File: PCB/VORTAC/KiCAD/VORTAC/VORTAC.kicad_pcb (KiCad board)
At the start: 2 copper layers, 46 x 52.4 mm, 12 parts, among them J1 MillMax_004, J11 STEPPER, J12 IO, J13 918-418K2023S40001, J2 MillMax_004, J3 DOCK, J4 USB_HOST, J5 FAN_01, J6 FAN_02, J7 LED, J8 HOTEND, U1 STM32F103C8Tx

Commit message: footprints and libs
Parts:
- moved U1 9.61 mm to (76.7, 117.3)

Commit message: Schematic and Lib Updates
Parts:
- added C11: 0.1uF, Capacitor_SMD:C_0402_1005Metric_Pad0.74x0.62mm_HandSolder, F.Cu at (76.4, 135.0)
- added D1: D, Diode_SMD:D_SOD-123F, F.Cu at (47.1, 89.1)
- added D2: D, Diode_SMD:D_SOD-123F, F.Cu at (55.6, 82.7)
- added D3: D, Diode_SMD:D_SOD-123F, F.Cu at (52.6, 89.1)
- added D4: D, Diode_SMD:D_SOD-123F, F.Cu at (55.7, 78.5)
- added IC1: TMC2209-LA-T, ToolChanger:tmc_2209_package, F.Cu at (85.6, 112.6)
- added J10: FAN_01_V, Connector_PinHeader_1.27mm:PinHeader_2x03_P1.27mm_Vertical, F.Cu at (69.1, 132.6)
- added J14: FAN_02_V, Connector_PinHeader_1.27mm:PinHeader_2x03_P1.27mm_Vertical, F.Cu at (74.4, 129.5)
- added J15: LED_V, Connector_PinHeader_1.27mm:PinHeader_2x03_P1.27mm_Vertical, F.Cu at (94.1, 129.8)
- added J16: THERM_R, Connector_PinHeader_1.27mm:PinHeader_2x03_P1.27mm_Vertical, F.Cu at (82.6, 130.1)
- added J9: Conn_02x03_Odd_Even, ToolChanger:Molex_Micro-Fit_3.0_43045-0612_2x03_P3.00mm_Vertical, F.Cu at (102.0, 110.7)
- added Q1: WSD4066DN, ToolChanger:WSD4066DN, F.Cu at (68.5, 111.3)
- added Q2: WSD4066DN, ToolChanger:WSD4066DN, F.Cu at (116.7, 91.1)
- added Q3: WSD4066DN, ToolChanger:WSD4066DN, F.Cu at (68.5, 125.8)
- added Q4: Q_NMOS_GSD, ToolChanger:IRF9310PbF-1_SO-8, F.Cu at (93.7, 122.5)
- added Q5: Q_NPN_BEC, Package_TO_SOT_SMD:SOT-23, F.Cu at (91.9, 104.6)
- added Q6: Q_PNP_BEC, Package_TO_SOT_SMD:SOT-23, F.Cu at (95.8, 104.5)
- added Q7: Q_NMOS_GSD, ToolChanger:IRF9310PbF-1_SO-8, F.Cu at (93.8, 109.3)
- added Q8: Q_PMOS_GSD, ToolChanger:IRF9310PbF-1_SO-8, F.Cu at (94.0, 115.1)
- added R1: 5.12K, Resistor_SMD:R_0402_1005Metric, F.Cu at (59.1, 108.7)
- added R10: 10K, Resistor_SMD:R_0402_1005Metric, F.Cu at (49.0, 126.3)
- added R11: 10K, Resistor_SMD:R_0402_1005Metric, F.Cu at (51.8, 110.7)
- added R12: 10K, Resistor_SMD:R_0402_1005Metric, F.Cu at (51.8, 112.7)
- added R13: 10K, Resistor_SMD:R_0402_1005Metric, F.Cu at (46.0, 122.9)
- added R14: 100R, Resistor_SMD:R_0402_1005Metric, F.Cu at (51.8, 114.6)
- added R15: 10K, Resistor_SMD:R_0402_1005Metric, F.Cu at (50.5, 118.4)
- added R2: 5.12K, Resistor_SMD:R_0402_1005Metric, F.Cu at (62.1, 108.7)
- added R22: 220K, Resistor_SMD:R_0402_1005Metric, F.Cu at (54.2, 85.4)
- added R23: 220K, Resistor_SMD:R_0402_1005Metric, F.Cu at (57.2, 85.4)
- added R24: 220K, Resistor_SMD:R_0402_1005Metric, F.Cu at (56.8, 87.4)
- added R25: 220K, Resistor_SMD:R_0402_1005Metric, F.Cu at (59.7, 87.4)
- added R26: 220K, Resistor_SMD:R_0402_1005Metric, F.Cu at (56.8, 89.3)
- added R27: 220K, Resistor_SMD:R_0402_1005Metric, F.Cu at (60.1, 85.4)
- added R28: 10K, Resistor_SMD:R_0402_1005Metric, F.Cu at (79.5, 135.0)
- added R3: 100R, Resistor_SMD:R_0402_1005Metric, F.Cu at (51.7, 126.5)
- added R4: 100R, Resistor_SMD:R_0402_1005Metric, F.Cu at (48.9, 122.9)
- added R5: 100R, Resistor_SMD:R_0402_1005Metric, F.Cu at (46.5, 108.9)
- added R6: 100R, Resistor_SMD:R_0402_1005Metric, F.Cu at (46.1, 126.3)
- added R7: 100R, Resistor_SMD:R_0402_1005Metric, F.Cu at (43.2, 126.3)
- added R8: 100R, Resistor_SMD:R_0402_1005Metric, F.Cu at (40.3, 127.5)
- added R9: 10K, Resistor_SMD:R_0402_1005Metric, F.Cu at (40.3, 125.5)
- added U2: ADXL343, Package_LGA:LGA-14_3x5mm_P0.8mm_LayoutBorder1x6y, F.Cu at (66.7, 142.6)
- moved J3 23.9 mm to (123.7, 89.6)
- moved J13 22.3 mm to (72.8, 103.7)
- moved U1 0.82 mm to (76.2, 117.9)
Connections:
- net MCU_D+ renamed USBMCU_D+
- net MCU_D- renamed USBMCU_D-
- J2 pad 4: HOST_VBUS -> Net-(J2-Pad4)
- J3 pad 1: V_IN -> Net-(J3-Pad1)
- J3 pad 2: CAN_H -> Net-(J3-Pad2)
- J3 pad 3: CAN_L -> Net-(J3-Pad3)
- J3 pad 4: TOOL_ID -> Net-(J3-Pad4)
- J3 pad 5: GND -> Net-(J3-Pad5)
- J4 pad 1: HOST_VBUS -> 5V
- J4 pad 2: HOST_D+ -> USBH_D+
- J4 pad 3: HOST_D- -> USBH_D-
- J4 pad 4: GND -> USBH_DRAIN
- J8 pad 1: THERM_1 -> V_IN
- J8 pad 2: V_IN -> HEATER_DRAIN
- J8 pad 3: GND -> THERM_1
- J8 pad 4: HEATER_DRAIN -> GND

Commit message: pushie
updates and stuff
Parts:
- removed Q2: WSD4066DN, ToolChanger:WSD4066DN
- added 10uH1: L, Inductor_SMD:L_Sunlord_MWSA0518_5.4x5.2mm, F.Cu at (76.8, 134.2)
- added 10uH2: L, Inductor_SMD:L_Sunlord_MWSA0518_5.4x5.2mm, F.Cu at (91.5, 134.2)
- added C1: 0.1uF, Capacitor_SMD:C_0402_1005Metric_Pad0.74x0.62mm_HandSolder, F.Cu at (101.0, 128.4)
- added C12: 10uF, Capacitor_SMD:C_1210_3225Metric, F.Cu at (81.6, 132.0)
- added C13: 0.1uF, Capacitor_SMD:C_0603_1608Metric, F.Cu at (72.9, 169.0)
- added C14: 0.1uF, Capacitor_SMD:C_0603_1608Metric, F.Cu at (72.2, 175.4)
- added C15: 0.1uF, Capacitor_SMD:C_0603_1608Metric, F.Cu at (72.9, 171.5)
- added C17: 0.1uF, Capacitor_SMD:C_0603_1608Metric, F.Cu at (68.4, 175.2)
- added C21: 47uF, Capacitor_SMD:C_0805_2012Metric, F.Cu at (68.6, 166.2)
- added C22: 47uF, Capacitor_SMD:C_0805_2012Metric, F.Cu at (68.6, 169.3)
- added C23: 47uF, Capacitor_SMD:C_0805_2012Metric, F.Cu at (72.6, 165.0)
- added C24: 47uF, Capacitor_SMD:C_0805_2012Metric, F.Cu at (68.6, 172.3)
- added R29: R_Small, Resistor_SMD:R_0402_1005Metric, F.Cu at (83.2, 160.7)
- added R30: 95k, Resistor_SMD:R_0402_1005Metric, F.Cu at (80.3, 162.7)
- added R31: 95k, Resistor_SMD:R_0402_1005Metric, F.Cu at (83.2, 162.7)
- added R32: 100k, Resistor_SMD:R_0402_1005Metric, F.Cu at (86.1, 160.7)
- added R33: 7.15k, Resistor_SMD:R_0402_1005Metric, F.Cu at (89.0, 160.7)
- added R34: 100k, Resistor_SMD:R_0402_1005Metric, F.Cu at (91.9, 160.7)
- added R35: 19.1k, Resistor_SMD:R_0402_1005Metric, F.Cu at (86.1, 162.7)
- added U3: TPS54335ADRCR, Package_SON:VSON-10-1EP_3x3mm_P0.5mm_EP1.65x2.4mm_ThermalVias, F.Cu at (81.8, 135.7)
- added U4: TPS54335ADRCR, Package_SON:VSON-10-1EP_3x3mm_P0.5mm_EP1.65x2.4mm_ThermalVias, F.Cu at (86.4, 135.8)
- C11: value 0.1uF -> 10uF; footprint Capacitor_SMD:C_0402_1005Metric_Pad0.74x0.62mm_HandSolder -> Capacitor_SMD:C_1210_3225Metric
- D1, D2, D3, D4: footprint Diode_SMD:D_SOD-123F -> Diode_SMD:D_SOD-923
- J16: footprint Connector_PinHeader_1.27mm:PinHeader_2x03_P1.27mm_Vertical -> Connector_PinHeader_1.27mm:PinHeader_2x02_P1.27mm_Vertical
- J3: value DOCK -> DEBUG; footprint Connector_JST:JST_PH_B5B-PH-K_1x05_P2.00mm_Vertical -> Connector_PinHeader_1.27mm:PinHeader_2x03_P1.27mm_Vertical
- R22, R23, R24, R25, R26, R27: value 220K -> 100K
- R28: value 10K -> R_Small
- R3: value 100R -> 1K .1%
- R4: value 100R -> 4.7K .1%
- moved J3 71.9 mm to (67.6, 134.5), turned to 0 degrees
- moved R9 60.7 mm to (100.9, 127.4)
- moved D3 53.8 mm to (98.3, 117.6), turned to 180 degrees
- moved R4 52.1 mm to (100.9, 125.4)
- moved D4 51.9 mm to (98.2, 108.2), turned to 180 degrees
- moved R24 50.7 mm to (98.3, 116.3), turned to 180 degrees
- moved D2 50.2 mm to (92.6, 116.6)
- moved R25 49.9 mm to (98.3, 118.9)
- moved R3 49.2 mm to (100.9, 126.4)
- moved D1 48.9 mm to (92.6, 107.2), turned to 180 degrees
- moved R23 48.2 mm to (92.7, 117.9)
- moved R27 45.0 mm to (98.1, 109.5)
- moved R26 44.9 mm to (98.1, 106.9)
- moved R22 44.9 mm to (92.8, 108.5), turned to 180 degrees
- moved J13 41.8 mm to (65.0, 144.8), turned to 270 degrees
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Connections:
- net TMC_BRA renamed Net-(IC1-Pad23)
- net TMC_BRB renamed Net-(IC1-Pad27)
- C11 pad 1: Net-(C11-Pad1) -> V_IN
- J10 pad 3: 5V -> 12V
- J10 pad 5: 3.3V -> 5V
- J11 pad 1: STEP_1_A1 -> STEP_1_A2
- J11 pad 2: STEP_1_A2 -> STEP_1_A1
- J14 pad 3: 5V -> 12V
- J14 pad 5: 3.3V -> 5V
- J15 pad 3: 5V -> 12V
- J15 pad 5: 3.3V -> 5V
- J16 pad 2: Net-(J16-Pad2) -> AREF
- J16 pad 4: Net-(J16-Pad4) -> AREF
- R3 pad 1: Net-(Q2-Pad2) -> Net-(J16-Pad1)
- R3 pad 2: HEATER_GATE -> THERM_1_PIN
- R4 pad 1: Net-(Q2-Pad4) -> Net-(J16-Pad3)
- R4 pad 2: HEATER_GATE -> THERM_1_PIN
- R9 pad 1: GND -> THERM_1
- R9 pad 2: HEATER_GATE -> THERM_1_PIN

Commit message: progress
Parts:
- removed Q8: Q_PMOS_GSD, ToolChanger:IRF9310PbF-1_SO-8
- removed R31: 95k, Resistor_SMD:R_0402_1005Metric
- added C10: 360pF, Capacitor_SMD:C_0603_1608Metric, F.Cu at (93.7, 123.6)
- added C16: 47uF, Capacitor_SMD:C_0805_2012Metric, F.Cu at (113.3, 107.7)
- added C18: 47uF, Capacitor_SMD:C_0805_2012Metric, F.Cu at (111.6, 107.7)
- added C19: 47uF, Capacitor_SMD:C_1206_3216Metric, F.Cu at (100.0, 108.6)
- added C2: 0.1uF, Capacitor_SMD:C_0402_1005Metric_Pad0.74x0.62mm_HandSolder, F.Cu at (117.5, 101.8)
- added C20: 47uF, Capacitor_SMD:C_0805_2012Metric, F.Cu at (109.8, 107.7)
- added C25: 470pF 100V, Capacitor_SMD:C_0603_1608Metric, F.Cu at (93.4, 78.2)
- added C26: 0.1uF 50V, Capacitor_SMD:C_0603_1608Metric, F.Cu at (96.9, 83.0)
- added C27: 470pF 100V, Capacitor_SMD:C_0603_1608Metric, F.Cu at (93.4, 75.6)
- added C28: 470pF 100V, Capacitor_SMD:C_0603_1608Metric, F.Cu at (106.8, 74.9)
- added C29: 0.1uF 50V, Capacitor_SMD:C_0603_1608Metric, F.Cu at (103.1, 83.0)
- added C3: 1uF, Capacitor_SMD:C_0603_1608Metric, F.Cu at (82.9, 111.0)
- added C30: 470pF 100V, Capacitor_SMD:C_0603_1608Metric, F.Cu at (106.6, 78.4)
- added C31: 100nF 16V, Capacitor_SMD:C_0603_1608Metric, F.Cu at (97.7, 81.7)
- added C33: 100nF 16V, Capacitor_SMD:C_0603_1608Metric, F.Cu at (102.3, 81.7)
- added C34: 100uF 35V, Capacitor_SMD:CP_Elec_8x6.9, F.Cu at (89.3, 86.8)
- added C4: 10uF, Capacitor_SMD:C_1206_3216Metric, F.Cu at (98.9, 117.5)
- added C5: 10uF, Capacitor_SMD:C_1206_3216Metric, F.Cu at (107.3, 117.5)
- added C6: 0.1uF, Capacitor_SMD:C_0603_1608Metric, F.Cu at (97.3, 116.8)
- added C7: 0.1uF, Capacitor_SMD:C_0603_1608Metric, F.Cu at (105.7, 116.8)
- added C8: 1uF, Capacitor_SMD:C_0603_1608Metric, F.Cu at (84.2, 111.0)
- added C9: 0.1uF, Capacitor_SMD:C_0603_1608Metric, F.Cu at (94.0, 115.2)
- added H1: M3, MountingHole:MountingHole_3mm_Pad_Via, F.Cu at (89.0, 78.0)
- added H2: M3, MountingHole:MountingHole_3mm_Pad_Via, F.Cu at (111.0, 78.0)
- added JP1: SolderJumper_2_Bridged, ToolChanger:SolderJumper_Hex_Bridged_Pad, B.Cu at (63.3, 92.9)
- added JP2: SolderJumper_2_Bridged, ToolChanger:SolderJumper_Hex_Bridged_Pad, B.Cu at (60.2, 91.1)
- added JP3: SolderJumper_2_Open, ToolChanger:SolderJumper_Hex_Open_Pad, B.Cu at (66.3, 91.1)
- added JP4: SolderJumper_2_Open, ToolChanger:SolderJumper_Hex_Open_Pad, B.Cu at (63.1, 89.3)
- added Q2: Q_NMOS_GSD, ToolChanger:IRF9310PbF-1_SO-8, F.Cu at (112.4, 89.7)
- added R16: 10K, Resistor_SMD:R_0402_1005Metric, F.Cu at (107.5, 96.4)
- added R17: 100K, Resistor_SMD:R_0402_1005Metric, F.Cu at (106.3, 88.0)
- added R18: 100K, Resistor_SMD:R_0402_1005Metric, F.Cu at (107.7, 88.4)
- added R19: 100K, Resistor_SMD:R_0402_1005Metric, F.Cu at (105.9, 82.6)
- added R20: 100K, Resistor_SMD:R_0402_1005Metric, F.Cu at (107.7, 82.6)
- added R21: 10K, Resistor_SMD:R_0402_1005Metric, F.Cu at (117.5, 100.8)
- added R36: 22R, Resistor_SMD:R_0402_1005Metric, F.Cu at (96.3, 103.1)
- added U5: ADXL345BCCZ-RL7, Package_LGA:LGA-14_3x5mm_P0.8mm_LayoutBorder1x6y, F.Cu at (83.6, 122.2)
- 10uH1, 10uH2: footprint Inductor_SMD:L_Sunlord_MWSA0518_5.4x5.2mm -> ToolChanger:L_Sunlord_MWSA0518_5.4x5.2mm
- C1: value 0.1uF -> 10uF 50V; footprint Capacitor_SMD:C_0402_1005Metric_Pad0.74x0.62mm_HandSolder -> Resistor_SMD:R_0603_1608Metric
- C11: value 10uF -> 0.1uF; footprint Capacitor_SMD:C_1210_3225Metric -> Capacitor_SMD:C_0603_1608Metric
- C12: value 10uF -> 3.3nF; footprint Capacitor_SMD:C_1210_3225Metric -> Capacitor_SMD:C_0603_1608Metric
- C13: value 0.1uF -> 30pF
- C14: value 0.1uF -> 56pF
- C15, C17: value 0.1uF -> 47uF; footprint Capacitor_SMD:C_0603_1608Metric -> Capacitor_SMD:C_1206_3216Metric
- C21, C22, C24: value 47uF -> 0.1uF 50V; footprint Capacitor_SMD:C_0805_2012Metric -> Capacitor_SMD:C_0603_1608Metric
- C23: value 47uF -> 22nF X7R 10% 50V; footprint Capacitor_SMD:C_0805_2012Metric -> Capacitor_SMD:C_0603_1608Metric
- IC1: value TMC2209-LA-T -> TMC2209-LA
- J1: value MillMax_004 -> DEBUG; footprint ToolChanger:MillMax-858-10-004-10-012000 -> Connector_PinHeader_1.27mm:PinHeader_2x03_P1.27mm_Vertical; moved to F.Cu
- J11: value STEPPER -> FAN_02_V; footprint Connector_JST:JST_PH_S4B-PH-K_1x04_P2.00mm_Horizontal -> Connector_PinHeader_1.27mm:PinHeader_2x03_P1.27mm_Vertical
- J12: value IO -> LED_V; footprint Connector_JST:JST_PH_B5B-PH-K_1x05_P2.00mm_Vertical -> Connector_PinHeader_1.27mm:PinHeader_2x03_P1.27mm_Vertical
- J13: value 918-418K2023S40001 -> THERM_R; footprint ToolChanger:USB_C_Receptacle_XKB_U262-16XN-4BVC11 -> Connector_PinHeader_1.27mm:PinHeader_2x02_P1.27mm_Vertical
- J14: value FAN_02_V -> 918-418K2023S40001; footprint Connector_PinHeader_1.27mm:PinHeader_2x03_P1.27mm_Vertical -> ToolChanger:USB_C_Receptacle_XKB_U262-16XN-4BVC11
- J15: value LED_V -> STEPPER; footprint Connector_PinHeader_1.27mm:PinHeader_2x03_P1.27mm_Vertical -> Connector_JST:JST_PH_S4B-PH-K_1x04_P2.00mm_Horizontal
- J16: value THERM_R -> IO; footprint Connector_PinHeader_1.27mm:PinHeader_2x02_P1.27mm_Vertical -> Connector_JST:JST_PH_B5B-PH-K_1x05_P2.00mm_Vertical
- J2: value MillMax_004 -> Molex Micro Fit 3.0; footprint ToolChanger:MillMax-858-10-004-10-012000 -> ToolChanger:Molex_Micro-Fit_3.0_43045-0612_2x03_P3.00mm_Vertical; moved to F.Cu
- J3: value DEBUG -> MillMax_004; footprint Connector_PinHeader_1.27mm:PinHeader_2x03_P1.27mm_Vertical -> ToolChanger:MillMax-858-10-004-10-012000; moved to B.Cu
- J4: value USB_HOST -> MillMax_004; footprint Connector_JST:JST_PH_B4B-PH-K_1x04_P2.00mm_Vertical -> ToolChanger:MillMax-858-10-004-10-012000; moved to B.Cu
- J5: value FAN_01 -> USB_HOST; footprint Connector_JST:JST_PH_B3B-PH-K_1x03_P2.00mm_Vertical -> Connector_JST:JST_PH_B4B-PH-K_1x04_P2.00mm_Vertical
- J6: value FAN_02 -> HOTEND; footprint Connector_JST:JST_PH_B3B-PH-K_1x03_P2.00mm_Vertical -> ToolChanger:Molex_Micro-Fit_3.0_43045-0412_2x02_P3.00mm_Vertical
- J7: value LED -> FAN_01; footprint Connector_JST:JST_PH_B2B-PH-K_1x02_P2.00mm_Vertical -> Connector_JST:JST_PH_B3B-PH-K_1x03_P2.00mm_Vertical
- J8: value HOTEND -> FAN_02; footprint ToolChanger:Molex_Micro-Fit_3.0_43045-0412_2x02_P3.00mm_Vertical -> Connector_JST:JST_PH_B3B-PH-K_1x03_P2.00mm_Vertical
- J9: value Conn_02x03_Odd_Even -> LED; footprint ToolChanger:Molex_Micro-Fit_3.0_43045-0612_2x03_P3.00mm_Vertical -> Connector_JST:JST_PH_B2B-PH-K_1x02_P2.00mm_Vertical
- Q1: value WSD4066DN -> Q_PMOS_GSD; footprint ToolChanger:WSD4066DN -> ToolChanger:IRF9310PbF-1_SO-8
- Q5: value Q_NPN_BEC -> WSD4066DN; footprint Package_TO_SOT_SMD:SOT-23 -> ToolChanger:WSD4066DN
- Q7: value Q_NMOS_GSD -> Q_NPN_BEC; footprint ToolChanger:IRF9310PbF-1_SO-8 -> Package_TO_SOT_SMD:SOT-23
- R1: value 5.12K -> 1K .1%
- R10, R11, R9: value 10K -> 100R
- R14: value 100R -> 10K
- R2: value 5.12K -> 4.7K .1%
- R22: value 100K -> 36.5k
- R23: value 100K -> 10k
- R24, R25: value 100K -> 95k
- R26: value 100K -> 100k
- R27: value 100K -> 7.15k
- R28: value R_Small -> 100k
- R29: value R_Small -> 19.1k
- R3: value 1K .1% -> 5.12K
- R30: value 95k -> 0.1R 1%; footprint Resistor_SMD:R_0402_1005Metric -> Resistor_SMD:R_1206_3216Metric
- R32: value 100k -> 22K
- R33: value 7.15k -> 22K
- R34: value 100k -> 0.1R 1%; footprint Resistor_SMD:R_0402_1005Metric -> Resistor_SMD:R_1206_3216Metric
- R35: value 19.1k -> 22R
- R4: value 4.7K .1% -> 5.12K
- R5, R6: value 100R -> 100K
- U1: value STM32F103C8Tx -> TLV73333PDBV; footprint Package_QFP:LQFP-48_7x7mm_P0.5mm -> Package_TO_SOT_SMD:SOT-23-5
- U2: value ADXL343 -> STM32F103C8Tx; footprint Package_LGA:LGA-14_3x5mm_P0.8mm_LayoutBorder1x6y -> Package_QFP:LQFP-48_7x7mm_P0.5mm
- moved C24 88.6 mm to (94.5, 87.5), turned to 90 degrees
- moved C21 86.3 mm to (103.9, 87.5), turned to 90 degrees
- moved R30 84.0 mm to (95.7, 80.2)
- moved C22 83.3 mm to (95.2, 90.3), turned to 180 degrees
- moved R34 81.4 mm to (103.7, 80.2), turned to 180 degrees
- moved C23 80.9 mm to (95.8, 87.5), turned to 90 degrees
- moved R2 76.5 mm to (117.5, 98.7)
- moved R32 75.9 mm to (95.8, 85.4), turned to 180 degrees
- moved J2 75.4 mm to (118.4, 84.1), turned to 90 degrees
- moved R1 74.5 mm to (117.5, 99.7)
- moved C17 71.8 mm to (100.0, 110.6)
- moved R33 71.4 mm to (101.4, 90.4), turned to 180 degrees
- moved C15 70.4 mm to (100.0, 106.5)
- moved J13 67.6 mm to (115.4, 99.7)
- moved C14 61.0 mm to (106.3, 124.8)
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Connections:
- net ADXL_AREF renamed Net-(U2-Pad6)
- net ADXL_CS renamed Net-(U2-Pad7)
- net ADXL_INT1 renamed Net-(U2-Pad8)
- net ADXL_SCL renamed Net-(U2-Pad14)
- net ADXL_SDI renamed USART_2_RX
- net ADXL_SDO renamed USART_2_TX
- C1 pad 1: THERM_1 -> V_IN
- C11 pad 1: V_IN -> Net-(10uH2-Pad1)
- C11 pad 2: GND -> Net-(C11-Pad2)
- C12 pad 1: V_IN -> Net-(C12-Pad1)
- C13 pad 1: V_IN -> Net-(C13-Pad1)
- C14 pad 1: V_IN -> Net-(C14-Pad1)
- C15 pad 1: Net-(10uH1-Pad1) -> 12V
- C15 pad 2: Net-(C15-Pad2) -> GND
- C17 pad 1: Net-(10uH2-Pad1) -> 12V
- C17 pad 2: Net-(C17-Pad2) -> GND
- C21 pad 1: 12V -> 3.3V
- C22 pad 1: 5V -> Net-(C22-Pad1)
- C23 pad 1: 12V -> Net-(C23-Pad1)
- C23 pad 2: GND -> Net-(C23-Pad2)
- C24 pad 1: 5V -> Net-(C24-Pad1)
- C24 pad 2: GND -> V_IN
- IC1 pad 13: Net-(IC1-Pad13) -> GND
- IC1 pad 22: TMC_VS -> V_IN
- IC1 pad 23: Net-(IC1-Pad23) -> TMC_BRA
- IC1 pad 27: Net-(IC1-Pad27) -> TMC_BRB
- IC1 pad 28: TMC_VS -> V_IN
- IC1 pad 4: Net-(C6-Pad2) -> Net-(C23-Pad2)
- IC1 pad 5: Net-(C6-Pad1) -> Net-(C23-Pad1)
- IC1 pad 6: Net-(C4-Pad1) -> Net-(C24-Pad1)
- IC1 pad 8: Net-(C3-Pad1) -> Net-(C22-Pad1)
- J1 pad 1: V_IN -> Net-(J1-Pad1)
- J1 pad 2: CAN_H -> Net-(J1-Pad2)
- J1 pad 3: CAN_L -> Net-(J1-Pad3)
- J1 pad 4: GND -> Net-(J1-Pad4)
- J11 pad 1: STEP_1_A2 -> V_IN
- J11 pad 2: STEP_1_A1 -> FAN_2_V_OUT
- J11 pad 3: STEP_1_B1 -> 12V
- J11 pad 4: STEP_1_B2 -> FAN_2_V_OUT
- J12 pad 1: 5V -> V_IN
- J12 pad 2: GND -> LED_1_V_OUT
- J12 pad 3: IO_1_OUT -> 12V
- J12 pad 4: IO_2_OUT -> LED_1_V_OUT
- J12 pad 5: IO_3_OUT -> 5V
- J15 pad 1: V_IN -> STEP_1_A2
- J15 pad 2: LED_1_V_OUT -> STEP_1_A1
- J15 pad 3: 12V -> STEP_1_B1
- J15 pad 4: LED_1_V_OUT -> STEP_1_B2
- J16 pad 1: Net-(J16-Pad1) -> 5V
- J16 pad 2: AREF -> GND
- J16 pad 3: Net-(J16-Pad3) -> IO_1_OUT
- J16 pad 4: AREF -> IO_2_OUT
- J2 pad 1: TOOL_ID -> TOOL_DATA_H
- J2 pad 2: HOST_D+ -> TOOL_DATA_L
- J2 pad 3: HOST_D- -> TOOL_ID
- J2 pad 4: Net-(J2-Pad4) -> GND
- J3 pad 1: Net-(J3-Pad1) -> TOOL_ID
- J3 pad 3: Net-(J3-Pad3) -> V_IN
- J3 pad 4: Net-(J3-Pad4) -> GND
- J4 pad 1: 5V -> HOST_USB_D-
- J4 pad 2: USBH_D+ -> HOST_USB_D+
- J4 pad 3: USBH_D- -> TOOL_DATA_H
- J4 pad 4: USBH_DRAIN -> TOOL_DATA_L
- J5 pad 1: FAN_1_DRAIN -> 5V
- J5 pad 2: FAN_1_TACHO -> HOST_USB_D+
- J5 pad 3: FAN_1_V_OUT -> HOST_USB_D-
- J6 pad 1: FAN_2_DRAIN -> V_IN
- J6 pad 2: FAN_2_TACHO -> THERM_1_OUT
- J6 pad 3: FAN_2_V_OUT -> HEATER_DRAIN
- J7 pad 1: LED_1_DRAIN -> FAN_1_DRAIN
- J7 pad 2: LED_1_V_OUT -> FAN_1_TACHO
- J8 pad 1: V_IN -> FAN_2_DRAIN
- J8 pad 2: HEATER_DRAIN -> FAN_2_TACHO
- J8 pad 3: THERM_1 -> FAN_2_V_OUT
- J9 pad 1: DOCK_V_IN -> LED_1_DRAIN
- J9 pad 2: DOCK_GND -> LED_1_V_OUT
- Q1 pad 1: GND -> Net-(D1-Pad1)
- Q1 pad 2: Net-(Q1-Pad2) -> V_IN
- Q1 pad 3: GND -> DOCK_V_IN
- Q3 pad 6: USBH_DRAIN -> HOST_USB_DRAIN
- Q5 pad 1: Net-(D4-Pad1) -> GND
- Q5 pad 3: Net-(D1-Pad1) -> GND
- Q7 pad 1: Net-(D2-Pad2) -> Net-(D4-Pad1)
- Q7 pad 2: GND -> Net-(Q7-Pad2)
- Q7 pad 3: DOCK_GND -> Net-(D1-Pad1)
- R1 pad 1: GND -> Net-(J13-Pad1)
- R1 pad 2: Net-(J13-PadB5) -> THERM_1_PIN
- R10 pad 1: GND -> Net-(Q5-Pad4)
- R10 pad 2: FAN_1_GATE -> FAN_2_GATE
- R11 pad 1: GND -> Net-(Q4-Pad1)
- R11 pad 2: FAN_2_GATE -> HEATER_GATE
- R14 pad 1: Net-(Q4-Pad1) -> GND
- R14 pad 2: HEATER_GATE -> FAN_1_GATE
- R15 pad 2: HEATER_GATE -> FAN_2_GATE
- R2 pad 1: GND -> Net-(J13-Pad3)
- R2 pad 2: Net-(J13-PadA5) -> THERM_1_PIN
- R22 pad 1: V_IN -> Net-(C13-Pad1)
- R22 pad 2: Net-(D1-Pad2) -> Net-(C10-Pad1)
- R23 pad 1: Net-(D2-Pad1) -> Net-(C14-Pad1)
- R23 pad 2: GND -> Net-(C12-Pad1)
- R24 pad 1: DOCK_V_IN -> GND
- R24 pad 2: Net-(Q6-Pad2) -> Net-(R24-Pad2)
- R25 pad 1: Net-(D3-Pad2) -> GND
- R25 pad 2: DOCK_GND -> Net-(R25-Pad2)
- R26 pad 1: Net-(Q5-Pad2) -> 12V
- R26 pad 2: DOCK_GND -> Net-(R26-Pad2)
- R27 pad 1: DOCK_V_IN -> Net-(R26-Pad2)
- R27 pad 2: Net-(D4-Pad1) -> GND
- R28 pad 1: Net-(C19-Pad1) -> 5V
- R28 pad 2: Net-(C16-Pad1) -> Net-(R28-Pad2)
- R29 pad 1: Net-(C20-Pad1) -> Net-(R28-Pad2)
- R29 pad 2: Net-(C18-Pad1) -> GND
- R3 pad 1: Net-(J16-Pad1) -> GND
- R3 pad 2: THERM_1_PIN -> Net-(J14-PadB5)
- R30 pad 2: Net-(R30-Pad2) -> TMC_BRB
- R32 pad 1: 12V -> TMC_ENN
- R32 pad 2: Net-(R32-Pad2) -> 3.3V
- R33 pad 1: Net-(R32-Pad2) -> TMC_UART_RX
- R34 pad 1: 5V -> GND
- R34 pad 2: Net-(R34-Pad2) -> TMC_BRA
- R35 pad 1: Net-(R34-Pad2) -> USB_D-
- R35 pad 2: GND -> Net-(R35-Pad2)
- R4 pad 1: Net-(J16-Pad3) -> GND
- R4 pad 2: THERM_1_PIN -> Net-(J14-PadA5)
- R5 pad 1: Net-(Q1-Pad2) -> V_IN
- R5 pad 2: FAN_1_GATE -> Net-(D1-Pad2)
- R6 pad 1: Net-(Q1-Pad4) -> Net-(D2-Pad1)
- R6 pad 2: FAN_2_GATE -> GND
- R9 pad 1: THERM_1 -> Net-(Q5-Pad2)
- R9 pad 2: THERM_1_PIN -> FAN_1_GATE
- U1 pad 1: Net-(U1-Pad1) -> 5V
- U1 pad 2: Net-(U1-Pad2) -> GND
- U1 pad 3: Net-(U1-Pad3) -> 5V
- U1 pad 5: Net-(U1-Pad5) -> 3.3V
- U2 pad 1: 3.3V -> Net-(U2-Pad1)
- U2 pad 2: GND -> Net-(U2-Pad2)
- U2 pad 4: GND -> Net-(U2-Pad4)
- U2 pad 5: GND -> Net-(U2-Pad5)
- U3 pad 10: Net-(R30-Pad2) -> Net-(R24-Pad2)
- U3 pad 6: Net-(R32-Pad2) -> Net-(R26-Pad2)
- U3 pad 7: Net-(C16-Pad1) -> Net-(C10-Pad1)
- U3 pad 9: Net-(C15-Pad2) -> Net-(C9-Pad2)
- U4 pad 10: Net-(R31-Pad2) -> Net-(R25-Pad2)
- U4 pad 6: Net-(R34-Pad2) -> Net-(R28-Pad2)
- U4 pad 7: Net-(C18-Pad1) -> Net-(C12-Pad1)
- U4 pad 9: Net-(C17-Pad2) -> Net-(C11-Pad2)
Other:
- outline, holes or cut-outs redrawn
- copper layers 2 -> 4

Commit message: progress
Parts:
- added C32: C_Small, Capacitor_SMD:C_0402_1005Metric, F.Cu at (81.5, 121.6)
- added C35: C_Small, Capacitor_SMD:C_0402_1005Metric, F.Cu at (95.4, 94.1)
- added D5: D_Schottky, Diode_SMD:D_SOD-123, F.Cu at (116.5, 123.6)
- added R31: 1K, Resistor_SMD:R_0402_1005Metric, F.Cu at (101.3, 90.6)
- added U6: TJA1040T, Package_SO:SOIC-8_3.9x4.9mm_P1.27mm, F.Cu at (99.7, 93.9)
- moved C33 5.60 mm to (106.6, 78.2)
- moved C31 5.59 mm to (93.4, 78.2)
- moved C22 3.00 mm to (98.2, 90.1), turned to 0 degrees
- moved U5 2.39 mm to (83.6, 119.8)
- moved C26 2.39 mm to (94.9, 81.7)
- moved C3 1.83 mm to (81.2, 111.7)
- moved C29 1.79 mm to (104.3, 81.7)
- moved C30 1.52 mm to (106.6, 76.9)
- moved C25 1.27 mm to (93.4, 76.9)
- moved U1 0.82 mm to (82.5, 114.7)
- moved C8 0.82 mm to (83.7, 111.7)
- moved C28 0.74 mm to (106.6, 75.6)
- moved R19 0.59 mm to (106.3, 82.2), turned to 90 degrees
- moved R33 0.58 mm to (101.3, 89.8)
- moved D1 0.43 mm to (104.3, 85.8)
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
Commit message: progress
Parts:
- U6: footprint Package_SO:SOIC-8_3.9x4.9mm_P1.27mm -> ToolChanger:SOIC-8_3.9x4.9mm_P1.27mm
- moved U6 15.1 mm to (112.4, 102.0)
- moved C35 14.7 mm to (108.1, 101.5)
- moved C1 12.2 mm to (107.4, 95.9)
- moved J13 6.20 mm to (116.3, 105.8), turned to 0 degrees
- moved R20 5.21 mm to (107.9, 87.8), turned to 180 degrees
- moved D4 5.19 mm to (107.9, 86.8), turned to 0 degrees
- moved D3 5.14 mm to (107.9, 92.6), turned to 180 degrees
- moved R18 5.00 mm to (107.9, 93.4), turned to 0 degrees
- moved R6 4.60 mm to (106.3, 93.9), turned to 270 degrees
- moved R1 4.32 mm to (117.5, 104.1)
- moved R2 4.32 mm to (117.5, 103.0)
- moved R5 3.94 mm to (106.3, 88.1), turned to 90 degrees
- moved C22 3.31 mm to (98.5, 93.4)
- moved R31 3.06 mm to (101.5, 93.7)
- moved R32 2.92 mm to (95.7, 88.3)
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
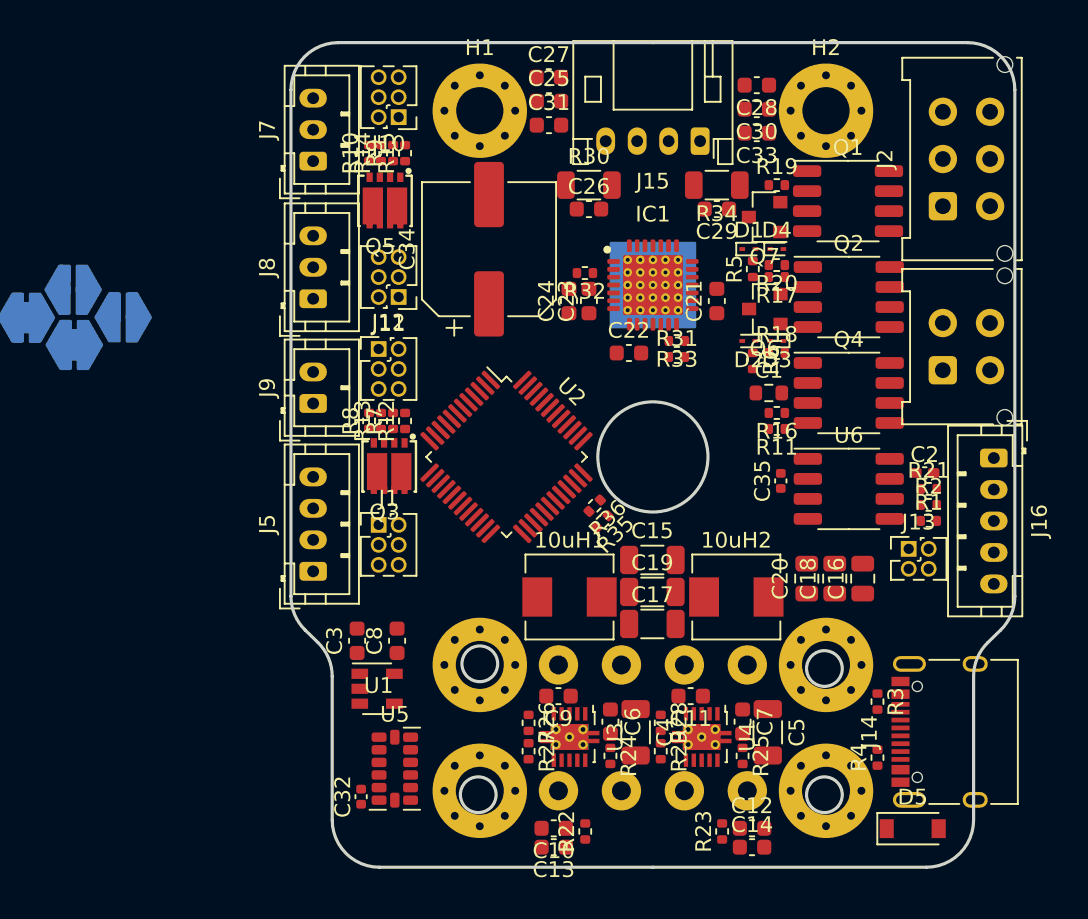
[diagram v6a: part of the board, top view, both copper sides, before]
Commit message: Layouting & Footprints
-Improved Thermal Footprint Conductivity
-Improved Component Spacing
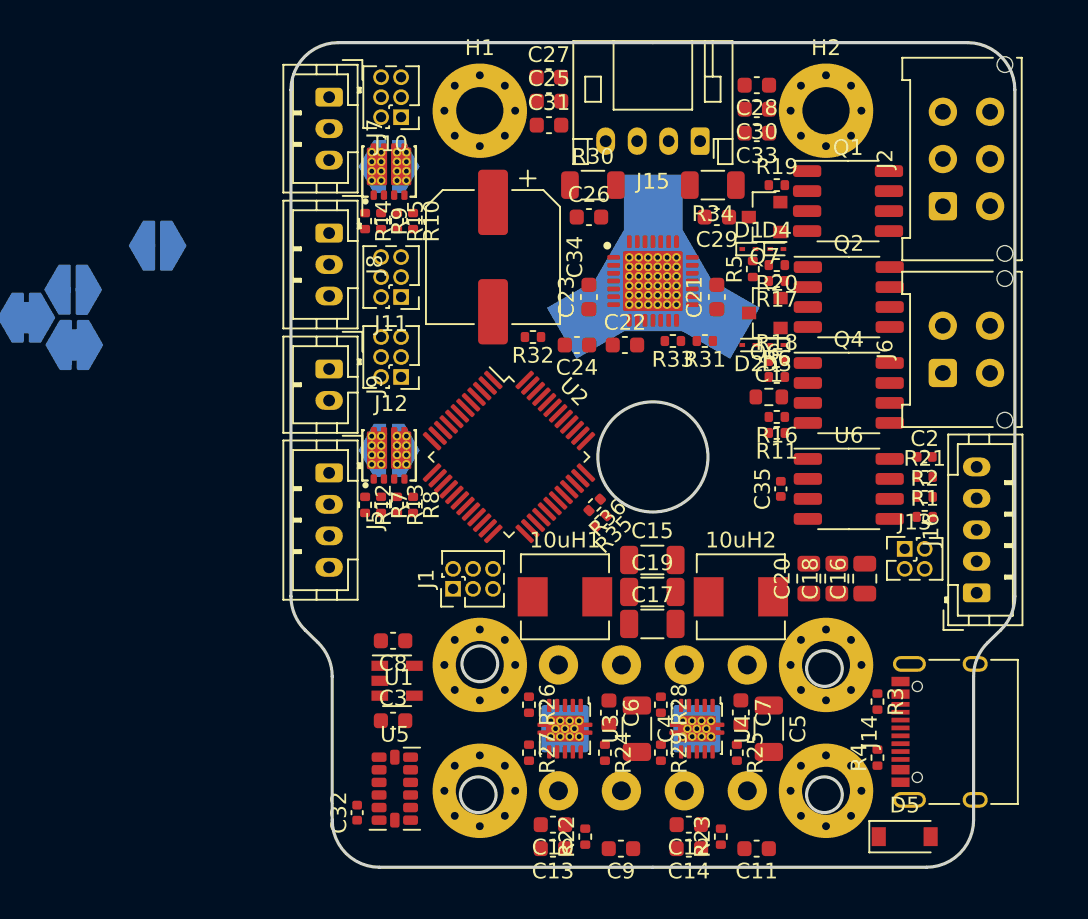
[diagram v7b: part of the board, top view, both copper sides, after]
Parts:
- C2: footprint Capacitor_SMD:C_0402_1005Metric_Pad0.74x0.62mm_HandSolder -> Capacitor_SMD:C_0402_1005Metric
- IC1: footprint ToolChanger:tmc_2209_package -> ToolChanger:tmc_2209_VORTAC
- Q3, Q5: footprint ToolChanger:WSD4066DN -> ToolChanger:WSD4066DN_ThermalPad
- U3, U4: footprint Package_SON:VSON-10-1EP_3x3mm_P0.5mm_EP1.65x2.4mm_ThermalVias -> ToolChanger:VSON-10-1EP_3x3mm_P0.5mm_EP1.65x2.4mm_ThermalVias
- moved C11 10.6 mm to (106.6, 124.9)
- moved C9 10.5 mm to (98.0, 124.9)
- moved J16 8.63 mm to (120.6, 108.6), turned to 90 degrees
- moved J5 6.34 mm to (79.4, 101.0), turned to 270 degrees
- moved J1 6.23 mm to (87.3, 108.4), turned to 90 degrees
- moved R8 6.02 mm to (84.8, 103.0), turned to 270 degrees
- moved R12 5.91 mm to (81.7, 103.0), turned to 270 degrees
- moved C3 5.57 mm to (83.5, 116.8), turned to 0 degrees
- moved R13 5.43 mm to (83.7, 103.0), turned to 270 degrees
- moved R7 5.39 mm to (82.7, 103.0), turned to 270 degrees
- moved R32 5.24 mm to (92.4, 92.4)
- moved R10 5.14 mm to (84.8, 85.0), turned to 270 degrees
- moved JP3 5.05 mm to (68.5, 86.5)
- moved R14 4.44 mm to (81.7, 85.0), turned to 270 degrees
- moved R9 4.39 mm to (82.7, 85.0), turned to 270 degrees
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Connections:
- J2 pad 1: TOOL_DATA_H -> GND
- J2 pad 2: TOOL_DATA_L -> DOCK_GND
- J2 pad 3: TOOL_ID -> DOCK_V_IN
- J2 pad 4: GND -> TOOL_DATA_L
- J2 pad 5: DOCK_GND -> TOOL_DATA_H
- J2 pad 6: DOCK_V_IN -> TOOL_ID
- J6 pad 1: V_IN -> HEATER_DRAIN
- J6 pad 2: THERM_1_OUT -> V_IN
- J6 pad 3: HEATER_DRAIN -> THERM_1_OUT
- Q3 pad 5: LED_1_DRAIN -> HOST_USB_DRAIN
- Q3 pad 6: HOST_USB_DRAIN -> LED_1_DRAIN
- Q5 pad 5: FAN_1_DRAIN -> FAN_2_DRAIN
- Q5 pad 6: FAN_2_DRAIN -> FAN_1_DRAIN
- R10 pad 2: FAN_2_GATE -> FAN_1_GATE
- R12 pad 2: LED_1_GATE -> USBH_GATE
- R13 pad 2: USBH_GATE -> LED_1_GATE
- R14 pad 2: FAN_1_GATE -> FAN_2_GATE
- R15 pad 2: FAN_2_GATE -> FAN_1_GATE
- R7 pad 2: LED_1_GATE -> USBH_GATE
- R8 pad 2: USBH_GATE -> LED_1_GATE
- R9 pad 2: FAN_1_GATE -> FAN_2_GATE
